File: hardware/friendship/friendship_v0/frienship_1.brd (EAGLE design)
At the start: 100 x 80 mm, 25 parts, among them T1 BCX70SMD, T2 BCX70SMD, T3 BCX70SMD, T4 BCX70SMD

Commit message: changes
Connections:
- removed net VCC: INTACK_LATCH.16, IRQ_LATCH.16, PRSNT_LATCH.16
- net 3V3: now also INTACK_LATCH.16, IRQ_LATCH.16, PRSNT_LATCH.16
- net GND: now also INTACK_LATCH.13
- net N$1: now also INTACK_LATCH.14; no longer INTACK_LATCH.13
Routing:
- net VCC: track 58.9 -> 0.00 mm, vias 3 -> 0
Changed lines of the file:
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@@
 <wire x1="35.5" y1="53.5" x2="36.9816" y2="53.5" width="0.4064" layer="16"/>
 <wire x1="36.9816" y1="53.5" x2="37.055" y2="53.4266" width="0.4064" layer="16"/>
+<contactref element="INTACK_LATCH" pad="8"/>
+<contactref element="PRSNT_LATCH" pad="8"/>
+<contactref element="IRQ_LATCH" pad="8"/>
+<contactref element="INTACK_LATCH" pad="13"/>
 <wire x1="75.73" y1="56" x2="78.27" y2="58.54" width="0" layer="19" extent="1-1"/>
-<wire x1="54.555" y1="53.4266" x2="75.73" y2="56" width="0" layer="19" extent="16-16"/>
+<wire x1="59.635" y1="59.5734" x2="75.73" y2="56" width="0" layer="19" extent="16-16"/>
+<wire x1="54.555" y1="53.4266" x2="59.635" y2="59.5734" width="0" layer="19" extent="16-16"/>
 <wire x1="37.055" y1="53.4266" x2="54.555" y2="53.4266" width="0" layer="19" extent="16-16"/>
 <wire x1="26.5" y1="31.5" x2="35.5" y2="53.5" width="0" layer="19" extent="16-16"/>
-</signal>
-<signal name="VCC">
-<contactref element="IRQ_LATCH" pad="16"/>
-<contactref element="PRSNT_LATCH" pad="16"/>
-<contactref element="INTACK_LATCH" pad="16"/>
-<wire x1="22.555" y1="50.9266" x2="21.0734" y2="50.9266" width="0.4064" layer="16"/>
-<wire x1="21.0734" y1="50.9266" x2="21" y2="51" width="0.4064" layer="16"/>
-<via x="21" y="51" extent="1-16" drill="0.5" diameter="1.016" shape="octagon"/>
-<wire x1="21" y1="51" x2="21" y2="58" width="0.4064" layer="1"/>
-<wire x1="21" y1="58" x2="25.5" y2="62.5" width="0.4064" layer="1"/>
-<wire x1="25.5" y1="62.5" x2="46" y2="62.5" width="0.4064" layer="1"/>
-<via x="46" y="62.5" extent="1-16" drill="0.5" diameter="1.016" shape="octagon"/>
-<wire x1="46" y1="62.5" x2="46" y2="59.5" width="0.4064" layer="16"/>
-<wire x1="63.445" y1="59.5734" x2="63.445" y2="62.445" width="0.4064" layer="16"/>
-<wire x1="63.445" y1="62.445" x2="63.5" y2="62.5" width="0.4064" layer="16"/>
-<via x="63.5" y="62.5" extent="1-16" drill="0.5" diameter="1.016" shape="octagon"/>
-<wire x1="63.5" y1="62.5" x2="46" y2="62.5" width="0.4064" layer="1"/>
-<wire x1="46" y1="59.5" x2="45.945" y2="59.5734" width="0" layer="19" extent="16-16"/>
 </signal>
 <signal name="TX-">
@@
 <wire x1="23" y1="53" x2="20.65" y2="53" width="0.4064" layer="16"/>
 <wire x1="20.65" y1="53" x2="20.5" y2="53.15" width="0.4064" layer="16"/>
+<wire x1="20.5" y1="53.15" x2="18.5" y2="53.15" width="0.4064" layer="16"/>
+<contactref element="INTACK_LATCH" pad="16"/>
+<contactref element="PRSNT_LATCH" pad="16"/>
+<contactref element="IRQ_LATCH" pad="16"/>
+<wire x1="56" y1="59.3984" x2="63.445" y2="59.5734" width="0" layer="19" extent="16-16"/>
+<wire x1="45.945" y1="59.5734" x2="44.675" y2="59.5734" width="0" layer="19" extent="16-16"/>
 <wire x1="23.825" y1="52.175" x2="44.675" y2="58.325" width="0" layer="19" extent="16-16"/>
-<wire x1="18.5" y1="31" x2="23.825" y2="50.9266" width="0" layer="19" extent="16-16"/>
-<wire x1="20.5" y1="53.15" x2="18.5" y2="53.15" width="0.4064" layer="16"/>
+<wire x1="22.555" y1="50.9266" x2="23.825" y2="50.9266" width="0" layer="19" extent="16-16"/>
+<wire x1="18.5" y1="31" x2="22.555" y2="50.9266" width="0" layer="19" extent="16-16"/>
 </signal>
 <signal name="5V">
@@
 </signal>
 <signal name="N$1">
-<contactref element="INTACK_LATCH" pad="13"/>
 <contactref element="BUSMASTER" pad="1"/>
-<wire x1="59.635" y1="59.5734" x2="78.27" y2="50.92" width="0" layer="19" extent="16-16"/>
+<contactref element="INTACK_LATCH" pad="14"/>
+<wire x1="60.905" y1="59.5734" x2="78.27" y2="50.92" width="0" layer="19" extent="16-16"/>
 </signal>
 <signal name="N$4">

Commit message: moar awesome
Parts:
- moved D1 18.9 mm to (31.0, 48.0), turned to 180 degrees
- moved D4 18.3 mm to (32.5, 44.5), turned to 90 degrees
- moved INTACK_LATCH 15.0 mm to (53.5, 42.5)
- moved R12 14.5 mm to (42.5, 48.0)
- moved PRSNT_LATCH 14.1 mm to (39.5, 42.5)
- moved D2 10.5 mm to (25.0, 43.0)
- moved D3 8.25 mm to (22.8, 46.0)
- moved R5 3.75 mm to (20.8, 51.0), turned to 90 degrees
- moved BUSMASTER 1.00 mm to (77.0, 57.0)
- moved R7 0.25 mm to (20.8, 54.0)
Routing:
- net TDI: track 16.7 -> 134.6 mm, vias 1 -> 2
- net N$11: track 0.00 -> 76.9 mm, vias 0 -> 2
- net GND: track 282.4 -> 359.1 mm, vias 19 -> 22
- net 3V3: track 109.8 -> 158.6 mm, vias 1 -> 5
- net PRSNT1: track 0.00 -> 31.2 mm, vias 0 -> 2
- net N$4: track 0.00 -> 24.9 mm
- net N$9: track 0.00 -> 23.2 mm
- net PRSNT0: track 24.3 -> 42.3 mm
- net N$1: track 0.00 -> 17.4 mm
- net /CS1: track 30.3 -> 15.0 mm, vias 2 -> 0
- net SHIFT: track 61.0 -> 47.2 mm, vias 0 -> 2
- net /CS0: track 47.1 -> 34.4 mm, vias 2 -> 0
- net N$3: track 61.4 -> 52.1 mm, vias 0 -> 2
- net /CS2: track 24.7 -> 16.4 mm
- net /CS3: track 41.9 -> 34.4 mm
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
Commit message: layout aimed at regular manufacturing processes
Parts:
- removed T1, T2, T3, T4: BCX70SMD, transistor:SOT23
- added IC5, IC6, IC7, IC8: 741G66DBV, 74xx-little-de:SOT23-5
- moved D2 12.5 mm to (23.1, 55.4)
- moved D4 12.3 mm to (23.2, 52.6), turned to 0 degrees
- moved D3 12.0 mm to (23.1, 58.0)
- moved R12 11.4 mm to (42.4, 59.4)
- moved R7 11.0 mm to (20.0, 65.0)
- moved INTACK_LATCH 10.6 mm to (53.4, 53.1)
- moved IRQ_LATCH 10.6 mm to (26.9, 64.6)
- moved PRSNT_LATCH 10.6 mm to (39.4, 53.1)
- moved R5 10.5 mm to (20.0, 61.5)
- moved D1 7.97 mm to (23.2, 49.9), turned to 0 degrees
- moved BUSMASTER 2.50 mm to (75.5, 59.0)
- moved R1 1.68 mm to (12.5, 30.8), turned to 90 degrees
- moved R4 1.01 mm to (73.4, 31.0)
- moved SJ1 0.62 mm to (94.0, 32.1), flipped to the bottom, turned to 180 degrees
- moved R2 0.50 mm to (32.5, 31.0)
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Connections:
- net 12V: now also PORT0.B10(+12V), PORT1.B10(+12V), PORT2.B10(+12V), PORT3.B10(+12V)
- net 3V3: now also IC5.5, IC6.5, IC7.5, IC8.5, PORT0.B06(+3V3), PORT1.B06(+3V3), PORT2.B06(+3V3), PORT3.B06(+3V3)
- net 5V: now also PORT0.B08(+5V), PORT1.B08(+5V), PORT2.B08(+5V), PORT3.B08(+5V)
- net GND: now also IC5.3, IC6.3, IC7.3, IC8.3, PORT0.B07(GND), PORT0.B09(GND), PORT0.B11(GND), PORT1.B07(GND), PORT1.B09(GND), PORT1.B11(GND), PORT2.B07(GND), PORT2.B09(GND), PORT2.B11(GND), PORT3.B07(GND), PORT3.B09(GND), PORT3.B11(GND); no longer BUSMASTER.7
- net N$1: now also BUSMASTER.3; no longer BUSMASTER.1
- net N$2: now also IC5.2, IC6.1; no longer T1.2, T2.3
- net N$3: now also BUSMASTER.1; no longer BUSMASTER.4
- net N$4: now also BUSMASTER.7; no longer BUSMASTER.3
- net N$6: now also IC6.2, IC8.1; no longer T2.2, T3.3
- net N$7: now also IC7.1, IC8.2; no longer T3.2, T4.3
- net PRSNT0: now also IC5.4; no longer T1.1
- net PRSNT1: now also IC6.4; no longer T2.1
- net PRSNT2: now also IC8.4; no longer T3.1
- net PRSNT3: now also IC7.4; no longer T4.1
- net TDI: now also IC5.1; no longer T1.3
- net TDO: now also IC7.2; no longer T4.2
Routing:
- net GND: track 359.1 -> 515.0 mm, vias 22 -> 8
- net 3V3: track 158.6 -> 241.5 mm, vias 5 -> 10
- net PRSNT3: track 26.7 -> 80.2 mm, vias 3 -> 2
- net TDI: track 134.6 -> 89.8 mm, vias 2 -> 0
- net PRSNT2: track 28.3 -> 59.8 mm
- net IRQ3: track 69.4 -> 84.3 mm, vias 0 -> 2
- net IRQ2: track 50.8 -> 65.6 mm, vias 0 -> 3
- net N$3: track 52.1 -> 66.6 mm
- net MOSI: track 79.0 -> 64.7 mm, vias 6 -> 0
- net PRSNT1: track 31.2 -> 45.2 mm
- net /CS: track 78.9 -> 65.0 mm, vias 6 -> 0
- net SHIFT: track 47.2 -> 61.0 mm
- net IRQ0: track 17.7 -> 30.0 mm
- net PRSNT0: track 42.3 -> 54.4 mm
- net RX+: track 72.9 -> 62.5 mm, vias 6 -> 0
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- added copper zone on layer 16, net GND

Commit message: added license information, top groundplane, minor routing cleanups
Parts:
- moved IC6 0.75 mm to (31.9, 22.6)
- moved IC8 0.38 mm to (51.6, 22.6)
- flipped SJ1 to the top, turned to 0 degrees
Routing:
- net GND: track 515.0 -> 571.8 mm, vias 8 -> 22
- net PRSNT3: track 80.2 -> 74.3 mm
- net PRSNT2: track 59.8 -> 54.5 mm
- net PRSNT1: track 45.2 -> 40.4 mm
- net N$2: track 33.7 -> 35.0 mm
- net 3V3: track 241.5 -> 242.4 mm
- added copper zone on layer 1, net GND
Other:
- board text added: "friendship0, (CC-BY-NC-SA 3.0) 2012, armin@hgg.aero, hadez@hgg.aero"

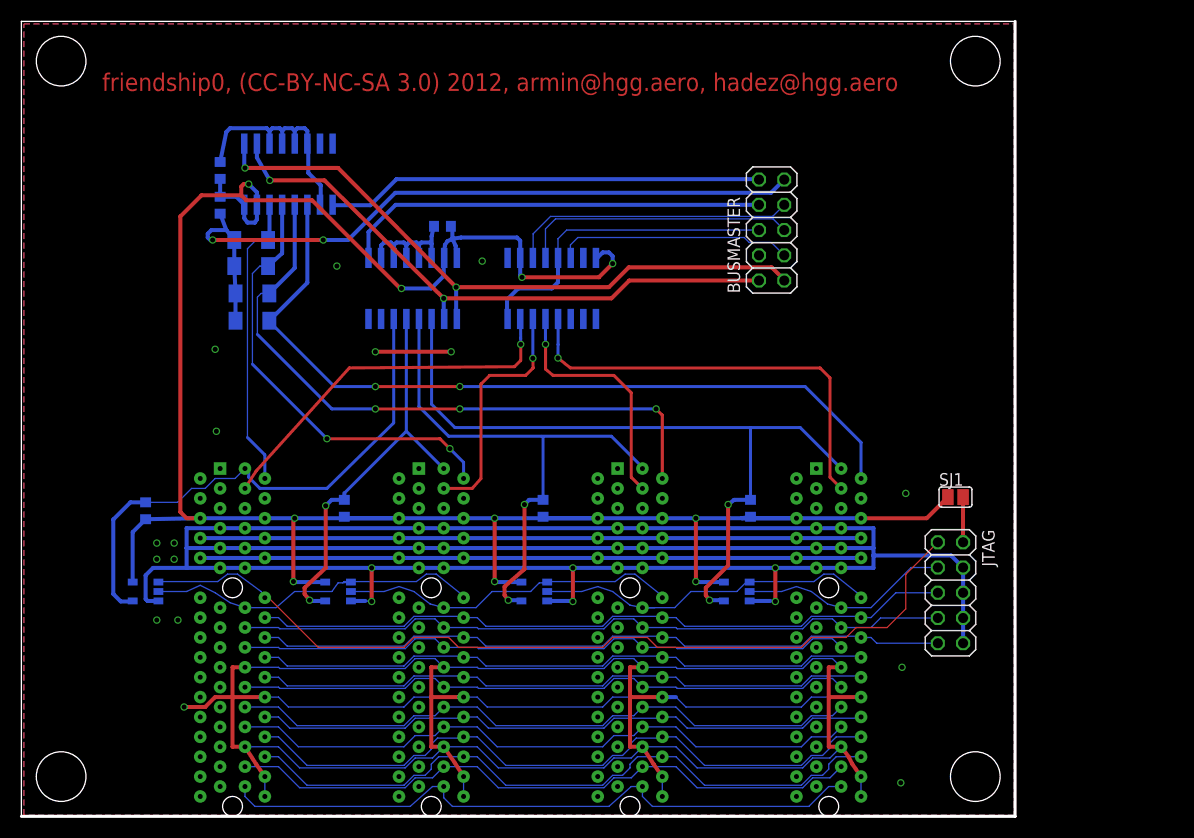
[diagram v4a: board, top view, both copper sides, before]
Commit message: added RS485 bus terminator resitors, onboard documentation / labelling
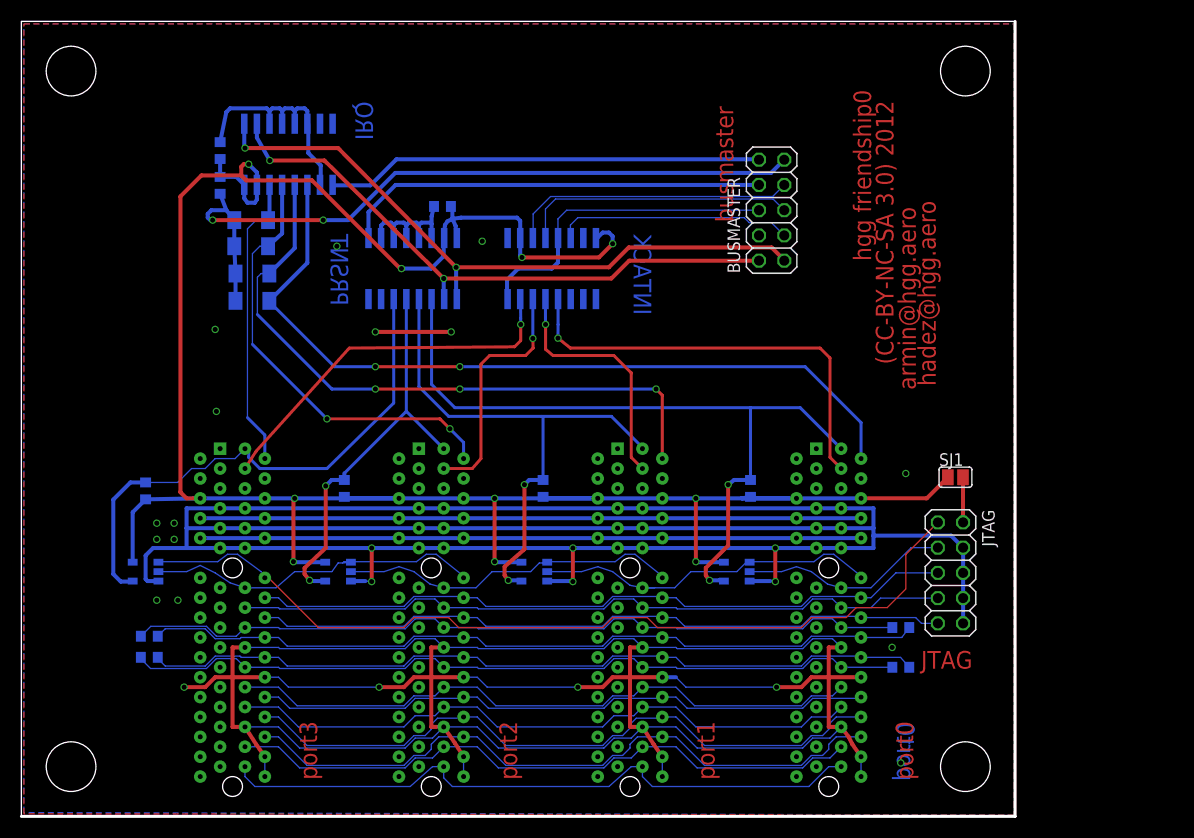
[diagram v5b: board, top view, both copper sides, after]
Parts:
- added R10, R6, R8, R9: 120, rcl:R0603
- moved BUSMASTER 2.00 mm to (75.5, 61.0)
- moved D1 2.00 mm to (23.2, 51.9)
- moved D2 2.00 mm to (23.1, 57.4)
- moved D3 2.00 mm to (23.1, 60.0)
- moved D4 2.00 mm to (23.2, 54.6)
- moved IC5 2.00 mm to (12.5, 24.6)
- moved IC6 2.00 mm to (31.9, 24.6)
- moved IC7 2.00 mm to (72.0, 24.6)
- moved IC8 2.00 mm to (51.6, 24.6)
- moved INTACK_LATCH 2.00 mm to (53.4, 55.1)
- moved IRQ_LATCH 2.00 mm to (26.9, 66.6)
- moved JTAG 2.00 mm to (93.5, 24.5)
- moved PORT0 2.00 mm to (20.0, 37.0)
- moved PORT1 2.00 mm to (40.0, 37.0)
- moved PORT2 2.00 mm to (60.0, 37.0)
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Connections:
- net RX+: now also R10.2, R8.2
- net RX-: now also R10.1, R8.1
- net TX+: now also R6.2, R9.2
- net TX-: now also R6.1, R9.1
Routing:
- net TX-: track 62.5 -> 79.7 mm
- net RX+: track 62.5 -> 79.5 mm
- net RX-: track 62.5 -> 79.4 mm
- net TX+: track 62.5 -> 79.4 mm
- net GND: track 571.8 -> 588.3 mm, vias 22 -> 25
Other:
- board text added: "(CC-BY-NC-SA 3.0) 2012"
- board text added: "INTACK"
- board text added: "IRQ"
- board text added: "JTAG"
- board text added: "PRSNT"
- board text added: "armin@hgg.aero"
- board text added: "busmaster"
- board text added: "hadez@hgg.aero"
- board text added: "hgg friendship0"
- board text added: "port0"
- board text added: "port1"
- board text added: "port2"
- board text added: "port3"
- board text removed: "friendship0, (CC-BY-NC-SA 3.0) 2012, armin@hgg.aero, hadez@hgg.aero"

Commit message: fixed wrong routing for differential bus pairs
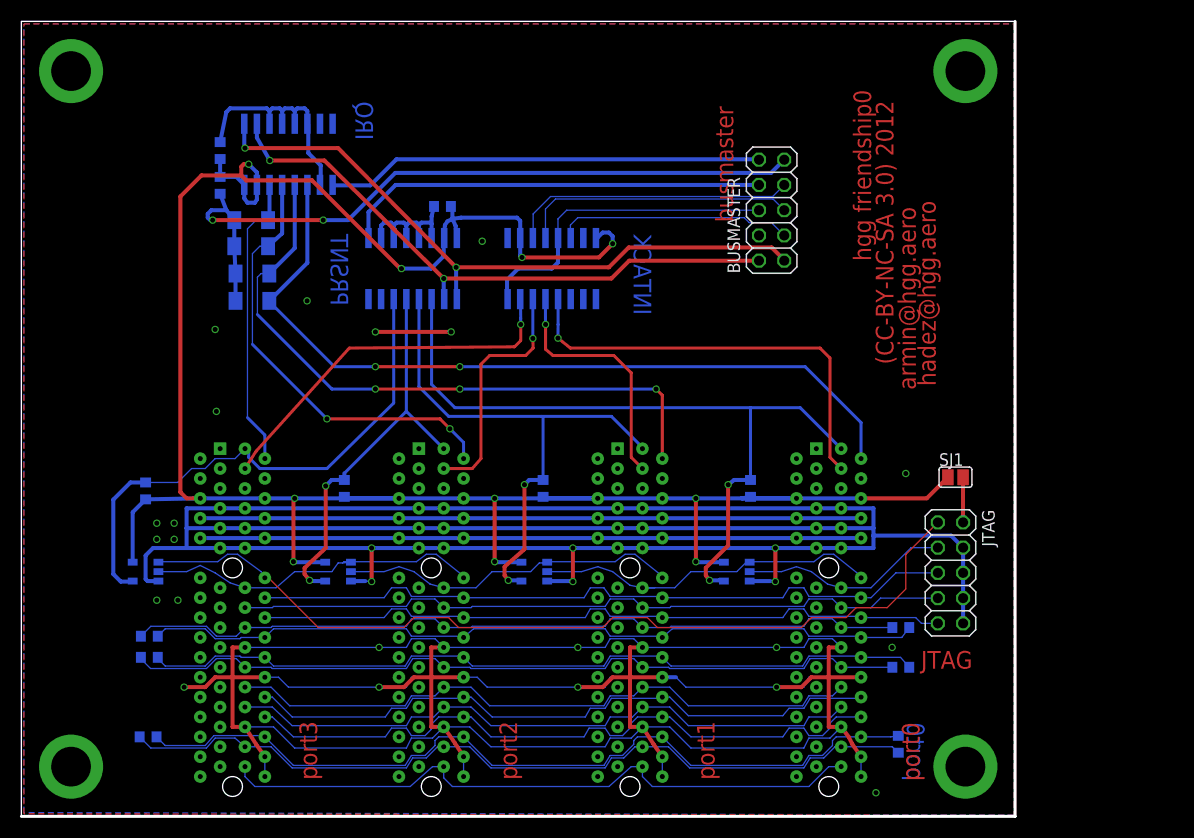
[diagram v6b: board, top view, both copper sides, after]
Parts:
- added R11, R13: 120, rcl:R0603
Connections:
- net FASTCLK+: now also R11.1, R13.1
- net FASTCLK-: now also R11.2, R13.2
- net RX+: now also PORT0.A20(BUS1+), PORT1.A20(BUS1+), PORT2.A20(BUS1+), PORT3.A20(BUS1+); no longer PORT0.A20(RX+), PORT1.A20(RX+), PORT2.A20(RX+), PORT3.A20(RX+)
- net RX-: now also PORT0.A21(BUS1-), PORT1.A21(BUS1-), PORT2.A21(BUS1-), PORT3.A21(BUS1-); no longer PORT0.A21(RX-), PORT1.A21(RX-), PORT2.A21(RX-), PORT3.A21(RX-)
- net TX+: now also PORT0.A18(BUS0+), PORT1.A18(BUS0+), PORT2.A18(BUS0+), PORT3.A18(BUS0+); no longer PORT0.A18(TX+), PORT1.A18(TX+), PORT2.A18(TX+), PORT3.A18(TX+)
- net TX-: now also PORT0.A17(BUS0-), PORT1.A17(BUS0-), PORT2.A17(BUS0-), PORT3.A17(BUS0-); no longer PORT0.A17(TX-), PORT1.A17(TX-), PORT2.A17(TX-), PORT3.A17(TX-)
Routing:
- net FASTCLK-: track 65.3 -> 83.5 mm
- net FASTCLK+: track 68.0 -> 83.9 mm
- net CLK: track 62.8 -> 65.5 mm
- net GND: track 588.3 -> 589.5 mm, vias 25 -> 32
- net TMS: track 71.3 -> 72.0 mm

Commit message: minor trace improvements
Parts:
- moved R2 0.25 mm to (32.5, 33.2)
- moved R3 0.25 mm to (52.5, 33.2)
- moved R4 0.25 mm to (73.4, 33.2)
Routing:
- net FASTCLK-: track 83.5 -> 82.1 mm
- net N$2: track 35.0 -> 33.7 mm
- net FASTCLK+: track 83.9 -> 82.6 mm
- net N$7: track 35.7 -> 36.5 mm
- net RX-: track 79.9 -> 79.2 mm
- net TX+: track 79.3 -> 78.7 mm
- net TX-: track 79.7 -> 79.1 mm
- net RX+: track 79.9 -> 79.3 mm
- net 3V3: track 242.4 -> 243.0 mm
- net CLK: track 65.5 -> 65.0 mm
- net MOSI: track 65.1 -> 64.6 mm
